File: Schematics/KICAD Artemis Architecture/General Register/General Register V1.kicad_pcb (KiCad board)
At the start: 4 copper layers, 61.6 x 32.5 mm, 25 parts, among them J1 Power, J2 Bus, J3 Control, J4 Current Value, U4 74LS173, U5 74LS173, U6 74LS245

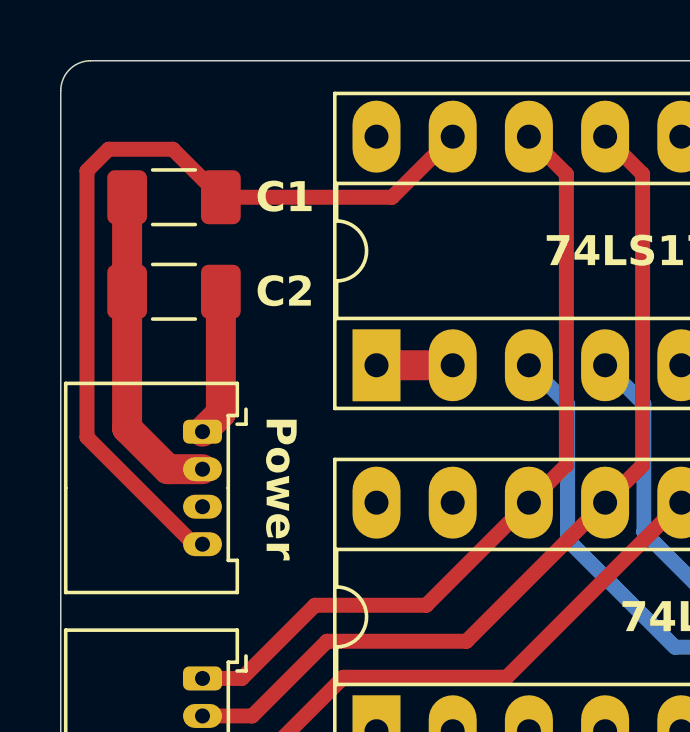
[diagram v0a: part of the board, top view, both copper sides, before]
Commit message: ALU PCB and Schematic Redesign
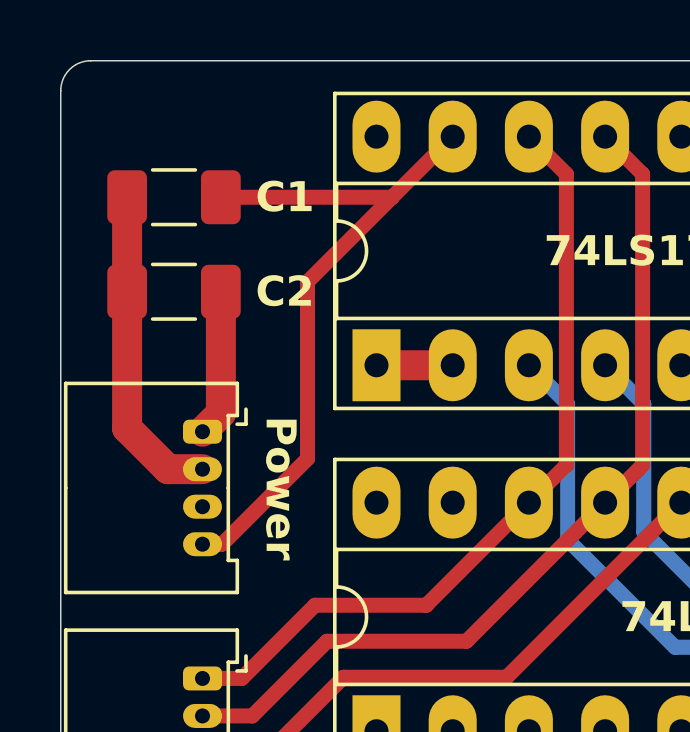
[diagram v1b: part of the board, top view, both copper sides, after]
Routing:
- net /CLR: track 52.1 -> 47.3 mm
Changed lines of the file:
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@@
 		)
 		(property "Value" "0.1uF"
-			(at 0 1.85 360)
+			(at 0 1.85 0)
 			(layer "F.Fab")
 			(effects
@@
 		)
 		(fp_text user "${REFERENCE}"
-			(at 0 0 360)
+			(at 0 0 0)
 			(layer "F.Fab")
 			(effects
@@
 		)
 		(property "Value" "0.1uF"
-			(at 0 1.85 360)
+			(at 0 1.85 0)
 			(layer "F.Fab")
 			(effects
@@
 		)
 		(fp_text user "${REFERENCE}"
-			(at 0 0 360)
+			(at 0 0 0)
 			(layer "F.Fab")
 			(effects
@@
 	(segment
 		(start 127.6625 57.8)
-		(end 126.0625 56.2)
+		(end 133.37 57.8)
 		(width 0.5)
 		(layer "F.Cu")
@@
 	)
 	(segment
-		(start 127.6625 57.8)
-		(end 133.37 57.8)
+		(start 127.05 69.365)
+		(end 127.7 69.365)
 		(width 0.5)
 		(layer "F.Cu")
@@
 	)
 	(segment
-		(start 123.91875 56.2)
-		(end 123.2 56.91875)
+		(start 130.55 66.515)
+		(end 130.55 60.62)
 		(width 0.5)
 		(layer "F.Cu")
@@
 	)
 	(segment
-		(start 126.0625 56.2)
-		(end 123.91875 56.2)
+		(start 127.7 69.365)
+		(end 130.55 66.515)
 		(width 0.5)
 		(layer "F.Cu")
@@
 	)
 	(segment
-		(start 123.2 56.91875)
-		(end 123.2 65.8)
+		(start 130.55 60.62)
+		(end 133.37 57.8)
 		(width 0.5)
 		(layer "F.Cu")
@@
 		(width 0.5)
 		(layer "F.Cu")
-		(net 30)
-	)
-	(segment
-		(start 123.2 65.8)
-		(end 126.765 69.365)
-		(width 0.5)
-		(layer "F.Cu")
